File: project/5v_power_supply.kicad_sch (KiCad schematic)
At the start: 6 parts, among them SW1 SW_SPST, U3 TPS61235P

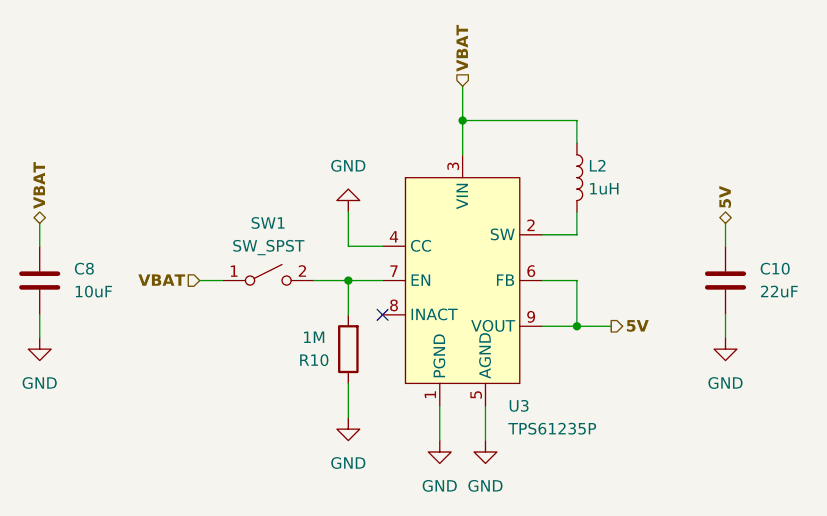
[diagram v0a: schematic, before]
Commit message: Added symbol annotations
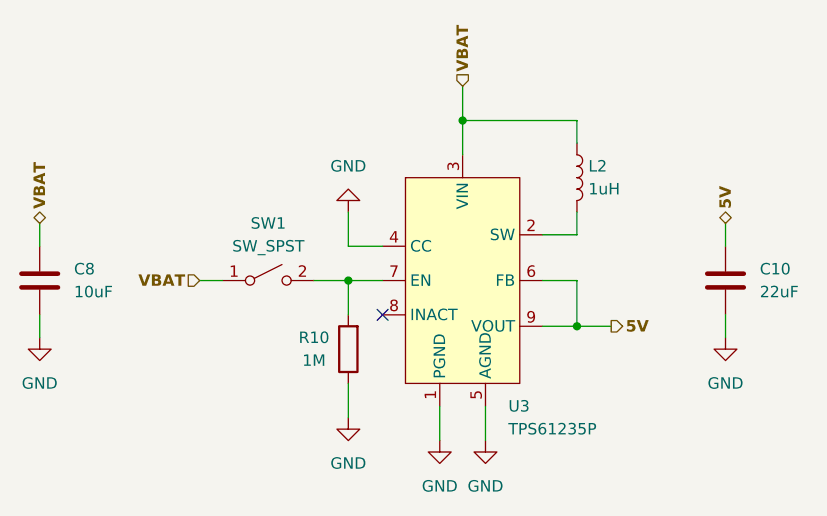
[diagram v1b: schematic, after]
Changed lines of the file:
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@@
         )
         (path "/d62f1157-7c2f-4dce-8167-d5624900d267/92ed0473-53e9-4211-a651-f912f1c2bd2b"
-          (reference "C3") (unit 1)
+          (reference "C7") (unit 1)
         )
       )
@@
         )
         (path "/d62f1157-7c2f-4dce-8167-d5624900d267/92ed0473-53e9-4211-a651-f912f1c2bd2b"
-          (reference "L1") (unit 1)
+          (reference "L2") (unit 1)
         )
       )
@@
   (symbol (lib_id "Device:R") (at 143.51 102.87 180) (unit 1)
     (in_bom yes) (on_board yes) (dnp no)
-    (property "Reference" "R10" (at 139.7 104.14 0)
-      (effects (font (size 1.27 1.27)))
-    )
-    (property "Value" "1M" (at 139.7 101.6 0)
+    (property "Reference" "R10" (at 139.7 101.6 0)
+      (effects (font (size 1.27 1.27)))
+    )
+    (property "Value" "1M" (at 139.7 104.14 0)
       (effects (font (size 1.27 1.27)))
     )
@@
         )
         (path "/d62f1157-7c2f-4dce-8167-d5624900d267/92ed0473-53e9-4211-a651-f912f1c2bd2b"
-          (reference "R4") (unit 1)
+          (reference "R5") (unit 1)
         )
       )
@@
         )
         (path "/d62f1157-7c2f-4dce-8167-d5624900d267/92ed0473-53e9-4211-a651-f912f1c2bd2b"
-          (reference "C4") (unit 1)
-        )
-      )
+          (reference "C8") (unit 1)
+        )
+      )

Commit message: Added footprints
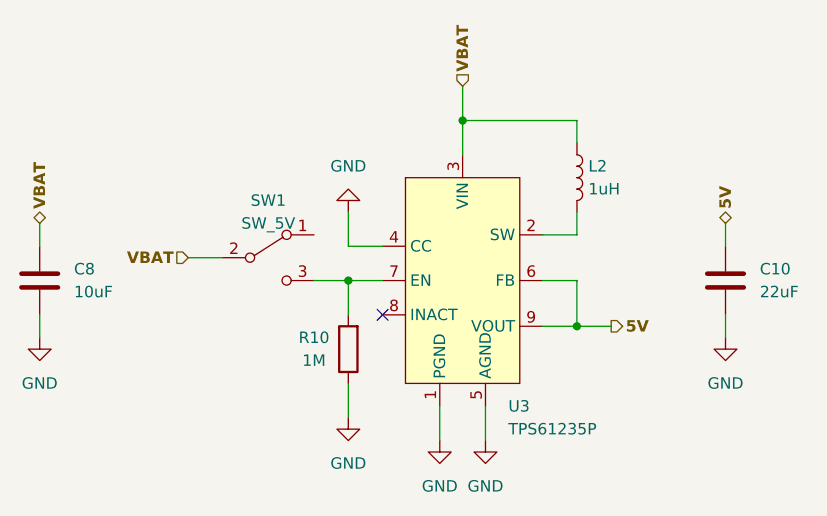
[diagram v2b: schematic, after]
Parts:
- R10: footprint Resistor_SMD:R_1210_3225Metric -> Resistor_SMD:R_0805_2012Metric
- SW1: value SW_SPST -> SW_5V; footprint (none) -> Button_Switch_SMD:SW_SPDT_PCM12; symbol Switch:SW_SPST -> Switch:SW_SPDT
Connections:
- net VBAT: now also SW1.2 (B); no longer SW1.1 (A)
- net at R10.2, U3.7 (EN): now also SW1.3 (C); no longer SW1.2 (B)
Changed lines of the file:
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@@
     (stroke (width 0) (type default))
   )
-  (wire (pts (xy 127 95.25) (xy 129.54 95.25))
+  (wire (pts (xy 125.73 92.71) (xy 129.54 92.71))
     (stroke (width 0) (type default))
   )
@@
     (effects (font (size 1.27 1.27) bold) (justify left))
   )
-  (hierarchical_label "VBAT" (shape input) (at 127 95.25 180) (fields_autoplaced)
+  (hierarchical_label "VBAT" (shape input) (at 125.73 92.71 180) (fields_autoplaced)
     (effects (font (size 1.27 1.27) bold) (justify right))
   )
@@
     )
   )
-  (symbol (lib_id "Switch:SW_SPST") (at 134.62 95.25 0) (unit 1)
-    (in_bom yes) (on_board yes) (dnp no) (fields_autoplaced)
-    (property "Reference" "SW1" (at 134.62 88.9 0)
-      (effects (font (size 1.27 1.27)))
-    )
-    (property "Value" "SW_SPST" (at 134.62 91.44 0)
-      (effects (font (size 1.27 1.27)))
-    )
-    (property "Footprint" "" (at 134.62 95.25 0)
-      (effects (font (size 1.27 1.27)) hide)
-    )
-    (property "Datasheet" "~" (at 134.62 95.25 0)
+  (symbol (lib_id "Switch:SW_SPDT") (at 134.62 92.71 0) (unit 1)
+    (in_bom yes) (on_board yes) (dnp no) (fields_autoplaced)
+    (property "Reference" "SW1" (at 134.62 86.36 0)
+      (effects (font (size 1.27 1.27)))
+    )
+    (property "Value" "SW_5V" (at 134.62 88.9 0)
+      (effects (font (size 1.27 1.27)))
+    )
+    (property "Footprint" "Button_Switch_SMD:SW_SPDT_PCM12" (at 134.62 92.71 0)
+      (effects (font (size 1.27 1.27)) hide)
+    )
+    (property "Datasheet" "~" (at 134.62 92.71 0)
       (effects (font (size 1.27 1.27)) hide)
     )
     (pin "1")
     (pin "2")
+    (pin "3")
     (instances
       (project "picoups"
@@
       (effects (font (size 1.27 1.27)))
     )
-    (property "Footprint" "Resistor_SMD:R_1210_3225Metric" (at 145.288 102.87 90)
-      (effects (font (size 1.27 1.27)) hide)
-    )
+    (property "Footprint" "Resistor_SMD:R_0805_2012Metric" (at 145.288 102.87 90)
+      (effects (font (size 1.27 1.27)) hide)
+    )

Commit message: Fixed footprint
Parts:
- SW1: footprint Button_Switch_SMD:SW_SPDT_PCM12 -> PicoUPS:SW_SPDT_PCM12
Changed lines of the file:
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@@
       (effects (font (size 1.27 1.27)))
     )
-    (property "Footprint" "Button_Switch_SMD:SW_SPDT_PCM12" (at 134.62 92.71 0)
+    (property "Footprint" "PicoUPS:SW_SPDT_PCM12" (at 134.62 92.71 0)
       (effects (font (size 1.27 1.27)) hide)
     )
